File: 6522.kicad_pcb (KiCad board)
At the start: 2 copper layers, 16 parts, among them J1 Conn_02x20_Top_Bottom, J2 Conn_02x01_Top_Bottom, P1 A2Bus, U1 74LS245, U2 74LS04, U3 74LS74, U4 W65C22, U5 W65C22

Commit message: more routing
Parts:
- moved C8 143.6 mm to (207.0, 58.8), turned to 270 degrees
- moved C7 135.3 mm to (204.8, 71.1), turned to 180 degrees
- moved C6 128.1 mm to (204.8, 91.4), turned to 180 degrees
- moved J2 108.8 mm to (203.8, 57.2), turned to 270 degrees
- moved U4 64.4 mm to (201.3, 91.4), turned to 270 degrees
- moved J1 40.7 mm to (201.3, 57.1), turned to 270 degrees
- moved U5 23.2 mm to (201.3, 71.1), turned to 270 degrees
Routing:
- net A0: track 0.00 -> 100.9 mm, vias 0 -> 2
- net A1: track 0.00 -> 100.3 mm, vias 0 -> 2
- net ~IRQ: track 0.00 -> 97.7 mm, vias 0 -> 3
- net A2: track 0.00 -> 96.8 mm, vias 0 -> 2
- net A3: track 0.00 -> 95.7 mm, vias 0 -> 2
- net R~W: track 0.00 -> 93.7 mm, vias 0 -> 3
- net D0: track 0.00 -> 74.5 mm, vias 0 -> 1
- net GND: track 81.8 -> 152.7 mm, vias 2 -> 4
- net D1: track 0.00 -> 69.6 mm, vias 0 -> 1
- net VCC: track 91.8 -> 160.9 mm, vias 0 -> 2
- net Net-(U2-Pad2): track 0.00 -> 68.3 mm, vias 0 -> 3
- net D2: track 0.00 -> 65.3 mm, vias 0 -> 1
- net ~RES: track 0.00 -> 63.1 mm
- net D3: track 0.00 -> 60.9 mm, vias 0 -> 1
- net D4: track 0.00 -> 56.9 mm, vias 0 -> 1
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
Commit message: routing complete
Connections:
- J1 pad 10: PB1 -> PC4
- J1 pad 11: PB2 -> PA5
- J1 pad 12: PB3 -> PC5
- J1 pad 13: PB4 -> PA6
- J1 pad 14: PB5 -> PC6
- J1 pad 15: PB6 -> PA7
- J1 pad 16: PB7 -> PC7
- J1 pad 17: CA1 -> PB0
- J1 pad 18: CA2 -> PD0
- J1 pad 19: CB1 -> PB1
- J1 pad 2: PA1 -> PC0
- J1 pad 20: CB2 -> PD1
- J1 pad 21: PC0 -> PB2
- J1 pad 22: PC1 -> PD2
- J1 pad 23: PC2 -> PB3
- J1 pad 24: PC3 -> PD3
- J1 pad 25: PC4 -> PB4
- J1 pad 26: PC5 -> PD4
- J1 pad 27: PC6 -> PB5
- J1 pad 28: PC7 -> PD5
- J1 pad 29: PD0 -> PB6
- J1 pad 3: PA2 -> PA1
- J1 pad 30: PD1 -> PD6
- J1 pad 31: PD2 -> PB7
- J1 pad 32: PD3 -> PD7
- J1 pad 33: PD4 -> CA1
- J1 pad 34: PD5 -> CC1
- J1 pad 35: PD6 -> CA2
- J1 pad 36: PD7 -> CC2
- J1 pad 37: CC1 -> CB1
- J1 pad 38: CC2 -> CD1
- J1 pad 39: CD1 -> CB2
- J1 pad 4: PA3 -> PC1
- J1 pad 5: PA4 -> PA2
- J1 pad 6: PA5 -> PC2
- J1 pad 7: PA6 -> PA3
- J1 pad 8: PA7 -> PC3
- J1 pad 9: PB0 -> PA4
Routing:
- net VCC: track 160.9 -> 251.6 mm
- net CA1: track 0.00 -> 83.4 mm
- net CA2: track 0.00 -> 81.8 mm
- net CC1: track 0.00 -> 60.9 mm
- net CC2: track 0.00 -> 60.2 mm
- net CB1: track 0.00 -> 36.5 mm
- net CB2: track 0.00 -> 36.4 mm
- net PB7: track 0.00 -> 35.9 mm, vias 0 -> 1
- net PB6: track 0.00 -> 35.3 mm
- net PB2: track 0.00 -> 35.3 mm
- net PA6: track 0.00 -> 35.3 mm
- net PA3: track 0.00 -> 35.3 mm
- net PB4: track 0.00 -> 35.3 mm
- net PB3: track 0.00 -> 35.3 mm
- net PA4: track 0.00 -> 35.3 mm
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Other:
- board outline added: 63.8 x 92.6 mm

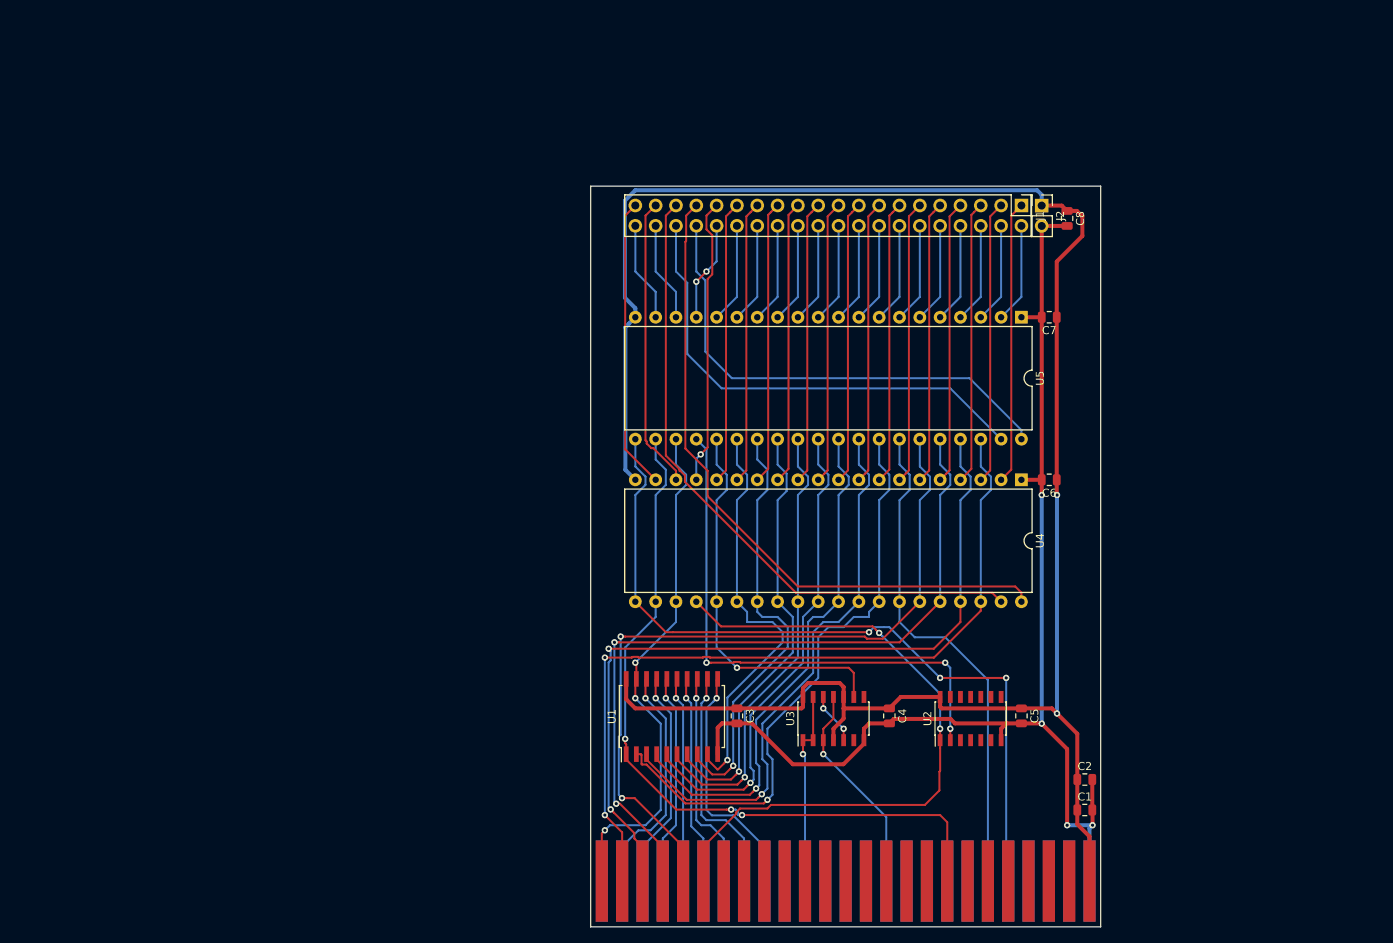
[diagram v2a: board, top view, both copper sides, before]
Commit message: shrink card a bit
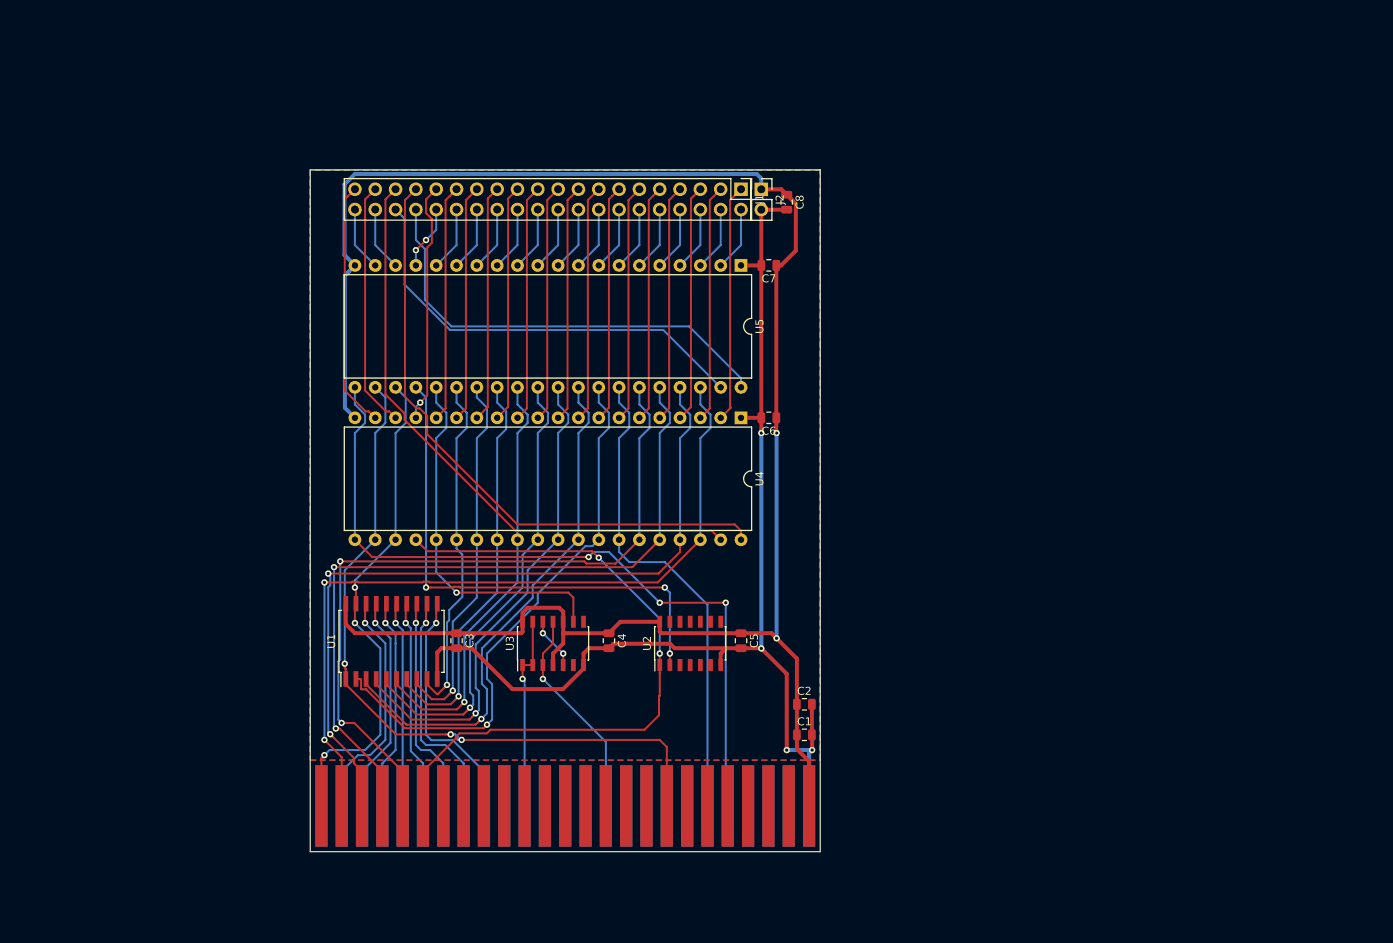
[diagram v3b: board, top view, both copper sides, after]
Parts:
- moved C3 36.3 mm to (130.7, 111.6)
- moved P1 36.3 mm to (144.3, 132.2)
- moved U3 36.3 mm to (142.7, 111.9)
- moved C1 36.3 mm to (174.2, 123.3)
- moved C2 36.3 mm to (174.2, 119.5)
- moved C4 36.3 mm to (149.7, 111.6)
- moved C5 36.3 mm to (166.2, 111.6)
- moved U1 36.3 mm to (122.6, 111.6)
- moved U2 36.3 mm to (159.9, 111.9)
- moved C6 35.9 mm to (169.7, 83.7)
- moved U4 35.9 mm to (166.2, 83.7)
- moved C7 35.6 mm to (169.7, 64.6)
- moved U5 35.6 mm to (166.2, 64.6)
- moved C8 35.1 mm to (172.0, 56.7)
- moved J1 35.1 mm to (166.2, 55.1)
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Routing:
- net VCC: track 251.6 -> 237.5 mm
- net D7: track 52.4 -> 43.5 mm
- net GND: track 152.7 -> 145.4 mm
- net D6: track 53.8 -> 46.6 mm
- net CA2: track 81.8 -> 76.1 mm
- net PB6: track 35.3 -> 29.6 mm
- net PB2: track 35.3 -> 29.6 mm
- net PA6: track 35.3 -> 29.6 mm
- net PA3: track 35.3 -> 29.6 mm
- net PB4: track 35.3 -> 29.6 mm
- net PB3: track 35.3 -> 29.6 mm
- net PA4: track 35.3 -> 29.6 mm
- net PB0: track 35.3 -> 29.6 mm
- net PA7: track 35.3 -> 29.6 mm
- net PA1: track 35.3 -> 29.6 mm
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- added copper zone on B.Cu, net (none)
- added copper zone on F.Cu, net (none)
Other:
- board size 63.8 x 92.6 mm -> 63.8 x 85.2 mm

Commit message: trim 150 mils off edge connector, generate gerbers
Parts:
- added REF**: OSHW-Symbol_8.9x8mm_SilkScreen, Symbol:OSHW-Symbol_8.9x8mm_SilkScreen, F.Cu at (165.7, 121.3)
- moved P1 1.91 mm to (144.3, 130.3)
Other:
- board size 63.8 x 85.2 mm -> 63.8 x 81.4 mm
- board text added: "Apple II Dual 6522 GPIO"
- board text added: "scott@alfter.us"

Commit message: add documentation
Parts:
- added G***: LOGO, qr:qr, B.Cu at (143.9, 115.3)
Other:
- board text added: "https://gitlab.com/salfter/a2gpio"

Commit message: add Schottky diodes on IRQ outputs for W65C22S
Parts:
- added D1: BAT54GW, Diode_SMD:D_SOD-123, F.Cu at (114.8, 98.3)
- added D2: BAT54GW, Diode_SMD:D_SOD-123, F.Cu at (114.9, 81.5)
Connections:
- U4 pad 21: ~IRQ -> Net-(D1-Pad1)
- U5 pad 21: ~IRQ -> Net-(D2-Pad1)
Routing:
- net Net-(D2-Pad1): track 0.00 -> 12.8 mm, vias 0 -> 1
- net Net-(D1-Pad1): track 0.00 -> 4.12 mm
- net A1: track 97.7 -> 96.9 mm

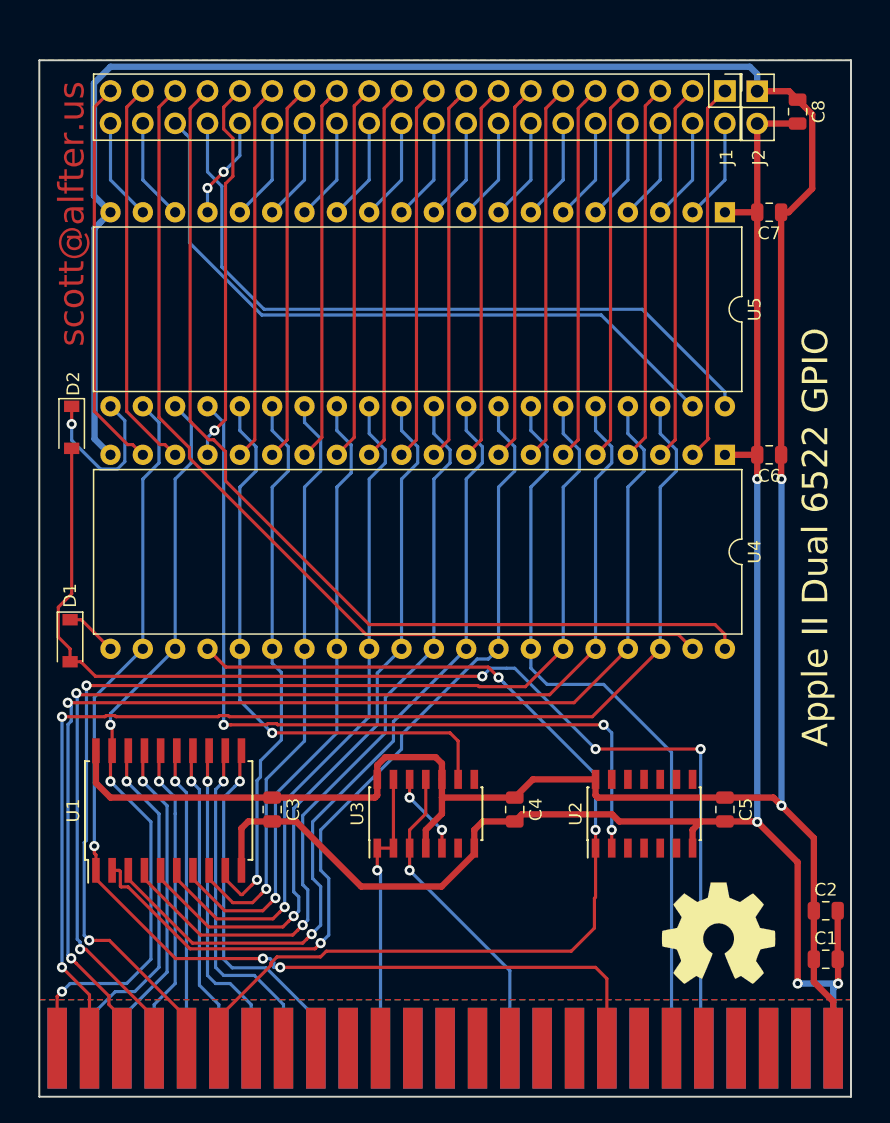
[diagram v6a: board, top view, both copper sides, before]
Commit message: edge connector revised
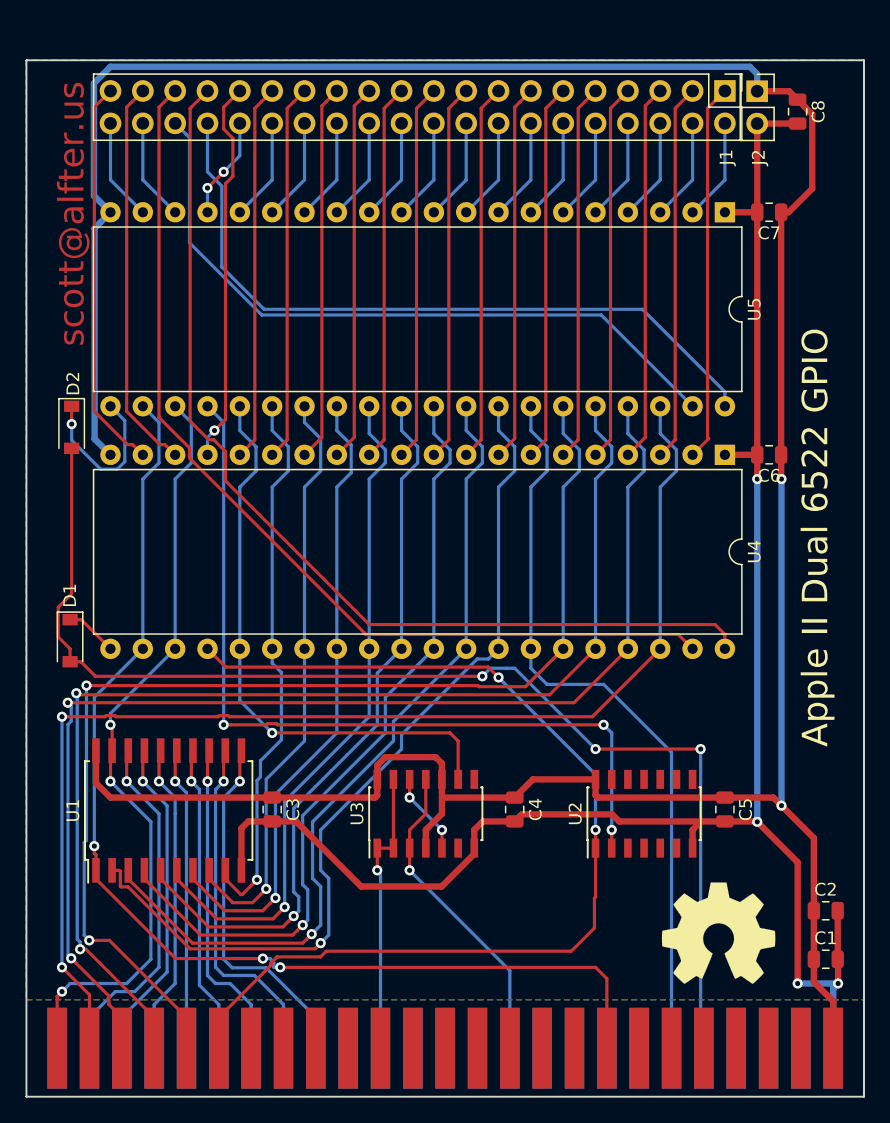
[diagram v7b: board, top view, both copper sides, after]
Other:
- board size 63.8 x 81.4 mm -> 65.8 x 81.4 mm
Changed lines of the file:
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@@
     (pad_drill 0.762)
     (pad_to_mask_clearance 0.2)
-    (aux_axis_origin 112.395 134.112)
+    (aux_axis_origin 111.379 134.112)
     (visible_elements 7FFFFFFF)
     (pcbplotparams
@@
       (effects (font (size 1.016 0.762) (thickness 0.127)))
     )
+    (fp_poly (pts (xy 32.893 -3.81) (xy 31.75 -3.81) (xy 31.75 3.81) (xy 32.893 3.81)) (layer F.Mask) (width 0.001))
+    (fp_poly (pts (xy 32.893 -3.81) (xy 31.75 -3.81) (xy 31.75 3.81) (xy 32.893 3.81)) (layer B.Mask) (width 0.001))
+    (fp_poly (pts (xy -32.893 -3.81) (xy -31.75 -3.81) (xy -31.75 3.81) (xy -32.893 3.81)) (layer F.Mask) (width 0.001))
+    (fp_poly (pts (xy -32.893 -3.81) (xy -31.75 -3.81) (xy -31.75 3.81) (xy -32.893 3.81)) (layer B.Mask) (width 0.001))
     (pad 50 smd rect (at -30.48 0 270) (size 6.35 1.524) (layers B.Cu B.Mask)
       (net 90 "Net-(P1-Pad50)") (solder_mask_margin 0.65) (clearance 0.254))
@@
     (effects (font (size 2 2) (thickness 0.4)))
   )
-  (gr_line (start 112.395 52.705) (end 112.395 134.112) (layer Edge.Cuts) (width 0.15))
-  (gr_line (start 176.149 52.705) (end 112.395 52.705) (layer Edge.Cuts) (width 0.15))
-  (gr_line (start 176.149 134.112) (end 176.149 52.705) (layer Edge.Cuts) (width 0.15))
-  (gr_line (start 112.395 134.112) (end 176.149 134.112) (layer Edge.Cuts) (width 0.15))
+  (gr_line (start 111.379 52.705) (end 111.379 134.112) (layer Edge.Cuts) (width 0.15))
+  (gr_line (start 111.379 52.705) (end 177.165 52.705) (layer Edge.Cuts) (width 0.15))
+  (gr_line (start 177.165 134.112) (end 177.165 52.705) (layer Edge.Cuts) (width 0.15))
+  (gr_line (start 111.379 134.112) (end 177.165 134.112) (layer Edge.Cuts) (width 0.15))
   (segment (start 163.703 83.693) (end 164.973 82.423) (width 0.25) (layer F.Cu) (net 1))
   (segment (start 164.973 56.388) (end 166.243 55.118) (width 0.25) (layer F.Cu) (net 1))
@@
     (polygon
       (pts
-        (xy 112.395 52.705) (xy 112.395 126.492) (xy 176.149 126.492) (xy 176.149 52.705)
+        (xy 111.379 52.705) (xy 111.379 126.492) (xy 177.165 126.492) (xy 177.165 52.705)
       )
     )
@@
     (polygon
       (pts
-        (xy 112.395 52.705) (xy 112.395 126.492) (xy 176.149 126.492) (xy 176.149 52.705)
+        (xy 111.379 52.705) (xy 111.379 126.492) (xy 177.165 126.492) (xy 177.165 52.705)
       )
     )
